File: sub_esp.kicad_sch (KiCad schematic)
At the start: 15 parts, among them J3 USB_C_Receptacle_USB2.0_14P, SW1 SW_Push, SW4 SW_Push, U6 ESP32-C3-WROOM-02, U7 BD33FC0FP

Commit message: 一部回路図変更と部品配置
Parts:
- C1: footprint Capacitor_SMD:C_0201_0603Metric_Pad0.64x0.40mm_HandSolder -> Capacitor_SMD:C_0603_1608Metric_Pad1.08x0.95mm_HandSolder
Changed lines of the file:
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@@
+					(unit 1)
+				)
+				(path "/537f457d-9719-41ea-89c7-39afb0f25936/8c87acd4-2081-458c-b251-53e233276ff2"
+					(reference "U11")
 					(unit 1)
 				)
@@
 					(unit 1)
 				)
+				(path "/537f457d-9719-41ea-89c7-39afb0f25936/8c87acd4-2081-458c-b251-53e233276ff2"
+					(reference "#PWR031")
+					(unit 1)
+				)
 			)
 		)
@@
 			)
 		)
-		(property "Footprint" "Capacitor_SMD:C_0201_0603Metric_Pad0.64x0.40mm_HandSolder"
+		(property "Footprint" "Capacitor_SMD:C_0603_1608Metric_Pad1.08x0.95mm_HandSolder"
 			(at 105.41 57.15 0)
 			(hide yes)
@@
 					(unit 1)
 				)
+				(path "/537f457d-9719-41ea-89c7-39afb0f25936/8c87acd4-2081-458c-b251-53e233276ff2"
+					(reference "C3")
+					(unit 1)
+				)
 			)
 		)
@@
 					(unit 1)
 				)
+				(path "/537f457d-9719-41ea-89c7-39afb0f25936/8c87acd4-2081-458c-b251-53e233276ff2"
+					(reference "R12")
+					(unit 1)
+				)
 			)
 		)
@@
 				(path "/537f457d-9719-41ea-89c7-39afb0f25936/1818fe2e-8d63-461c-a592-c1a19b493a42"
 					(reference "R2")
+					(unit 1)
+				)
+				(path "/537f457d-9719-41ea-89c7-39afb0f25936/8c87acd4-2081-458c-b251-53e233276ff2"
+					(reference "R10")
 					(unit 1)
 				)
@@
 					(unit 1)
 				)
+				(path "/537f457d-9719-41ea-89c7-39afb0f25936/8c87acd4-2081-458c-b251-53e233276ff2"
+					(reference "U10")
+					(unit 1)
+				)
 			)
 		)
@@
 					(unit 1)
 				)
+				(path "/537f457d-9719-41ea-89c7-39afb0f25936/8c87acd4-2081-458c-b251-53e233276ff2"
+					(reference "C4")
+					(unit 1)
+				)
 			)
 		)
@@
 					(unit 1)
 				)
+				(path "/537f457d-9719-41ea-89c7-39afb0f25936/8c87acd4-2081-458c-b251-53e233276ff2"
+					(reference "R14")
+					(unit 1)
+				)
 			)
 		)
@@
 				(path "/537f457d-9719-41ea-89c7-39afb0f25936/1818fe2e-8d63-461c-a592-c1a19b493a42"
 					(reference "R3")
+					(unit 1)
+				)
+				(path "/537f457d-9719-41ea-89c7-39afb0f25936/8c87acd4-2081-458c-b251-53e233276ff2"
+					(reference "R13")
 					(unit 1)
 				)
@@
 					(unit 1)
 				)
+				(path "/537f457d-9719-41ea-89c7-39afb0f25936/8c87acd4-2081-458c-b251-53e233276ff2"
+					(reference "#PWR041")
+					(unit 1)
+				)
 			)
 		)
@@
 					(unit 1)
 				)
+				(path "/537f457d-9719-41ea-89c7-39afb0f25936/8c87acd4-2081-458c-b251-53e233276ff2"
+					(reference "#PWR052")
+					(unit 1)
+				)
 			)
 		)
@@
 					(unit 1)
 				)
+				(path "/537f457d-9719-41ea-89c7-39afb0f25936/8c87acd4-2081-458c-b251-53e233276ff2"
+					(reference "#PWR042")
+					(unit 1)
+				)
 			)
 		)
@@
 					(unit 1)
 				)
+				(path "/537f457d-9719-41ea-89c7-39afb0f25936/8c87acd4-2081-458c-b251-53e233276ff2"
+					(reference "J4")
+					(unit 1)
+				)
 			)
 		)
@@
 					(unit 1)
 				)
+				(path "/537f457d-9719-41ea-89c7-39afb0f25936/8c87acd4-2081-458c-b251-53e233276ff2"
+					(reference "SW8")
+					(unit 1)
+				)
 			)
 		)
@@
 				(path "/537f457d-9719-41ea-89c7-39afb0f25936/1818fe2e-8d63-461c-a592-c1a19b493a42"
 					(reference "R1")
+					(unit 1)
+				)
+				(path "/537f457d-9719-41ea-89c7-39afb0f25936/8c87acd4-2081-458c-b251-53e233276ff2"
+					(reference "R9")
 					(unit 1)
 				)
@@
 					(unit 1)
 				)
+				(path "/537f457d-9719-41ea-89c7-39afb0f25936/8c87acd4-2081-458c-b251-53e233276ff2"
+					(reference "#PWR040")
+					(unit 1)
+				)
 			)
 		)
@@
 					(unit 1)
 				)
+				(path "/537f457d-9719-41ea-89c7-39afb0f25936/8c87acd4-2081-458c-b251-53e233276ff2"
+					(reference "#PWR039")
+					(unit 1)
+				)
 			)
 		)
@@
 					(unit 1)
 				)
+				(path "/537f457d-9719-41ea-89c7-39afb0f25936/8c87acd4-2081-458c-b251-53e233276ff2"
+					(reference "#PWR034")
+					(unit 1)
+				)
 			)
 		)
@@
 					(unit 1)
 				)
+				(path "/537f457d-9719-41ea-89c7-39afb0f25936/8c87acd4-2081-458c-b251-53e233276ff2"
+					(reference "D7")
+					(unit 1)
+				)
 			)
 		)
@@
 					(unit 1)
 				)
+				(path "/537f457d-9719-41ea-89c7-39afb0f25936/8c87acd4-2081-458c-b251-53e233276ff2"
+					(reference "#PWR044")
+					(unit 1)
+				)
 			)
 		)
@@
 					(unit 1)
 				)
+				(path "/537f457d-9719-41ea-89c7-39afb0f25936/8c87acd4-2081-458c-b251-53e233276ff2"
+					(reference "SW7")
+					(unit 1)
+				)
 			)
 		)
@@
 					(unit 1)
 				)
+				(path "/537f457d-9719-41ea-89c7-39afb0f25936/8c87acd4-2081-458c-b251-53e233276ff2"
+					(reference "#PWR051")
+					(unit 1)
+				)
 			)
 		)
@@
 				(path "/537f457d-9719-41ea-89c7-39afb0f25936/1818fe2e-8d63-461c-a592-c1a19b493a42"
 					(reference "C25")
+					(unit 1)
+				)
+				(path "/537f457d-9719-41ea-89c7-39afb0f25936/8c87acd4-2081-458c-b251-53e233276ff2"
+					(reference "C27")
 					(unit 1)
 				)
@@
 					(unit 1)
 				)
+				(path "/537f457d-9719-41ea-89c7-39afb0f25936/8c87acd4-2081-458c-b251-53e233276ff2"
+					(reference "C28")
+					(unit 1)
+				)
 			)
 		)
@@
 					(unit 1)
 				)
+				(path "/537f457d-9719-41ea-89c7-39afb0f25936/8c87acd4-2081-458c-b251-53e233276ff2"
+					(reference "#PWR050")
+					(unit 1)
+				)
 			)
 		)
@@
 					(unit 1)
 				)
+				(path "/537f457d-9719-41ea-89c7-39afb0f25936/8c87acd4-2081-458c-b251-53e233276ff2"
+					(reference "#PWR032")
+					(unit 1)
+				)

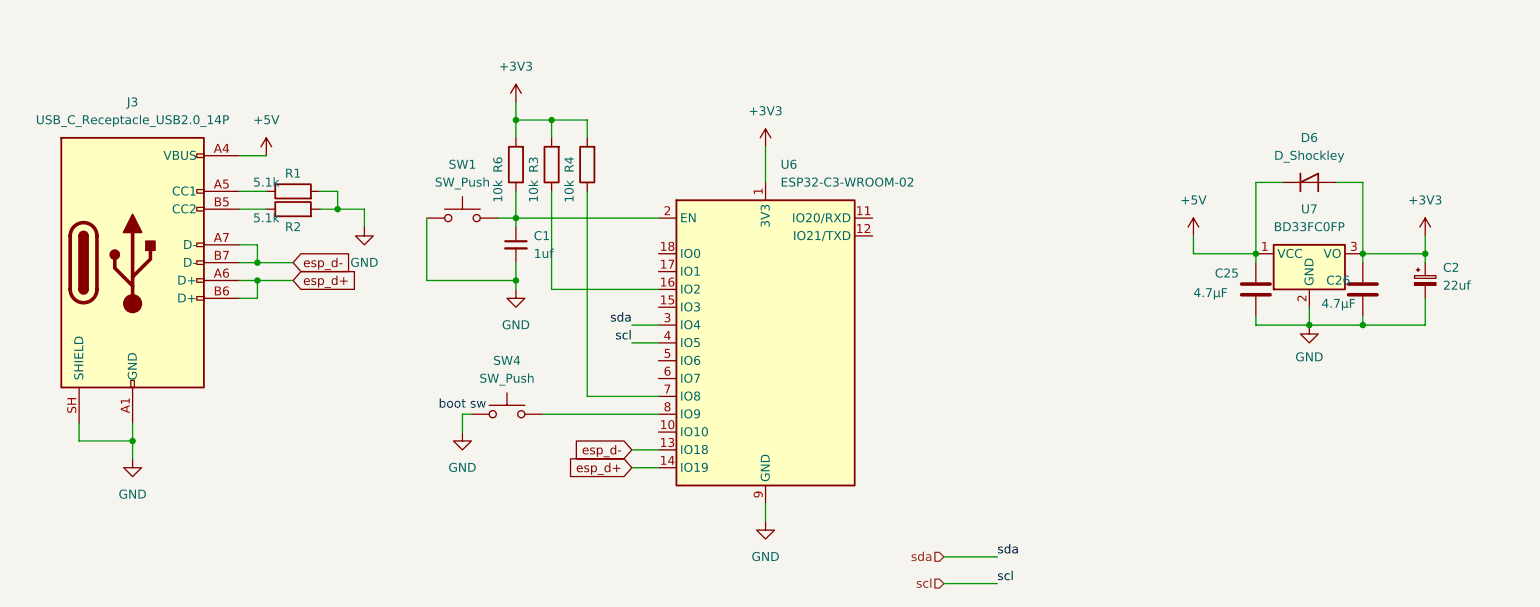
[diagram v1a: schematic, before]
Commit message: 完成(電磁弁制御,モーター出力追加済み)
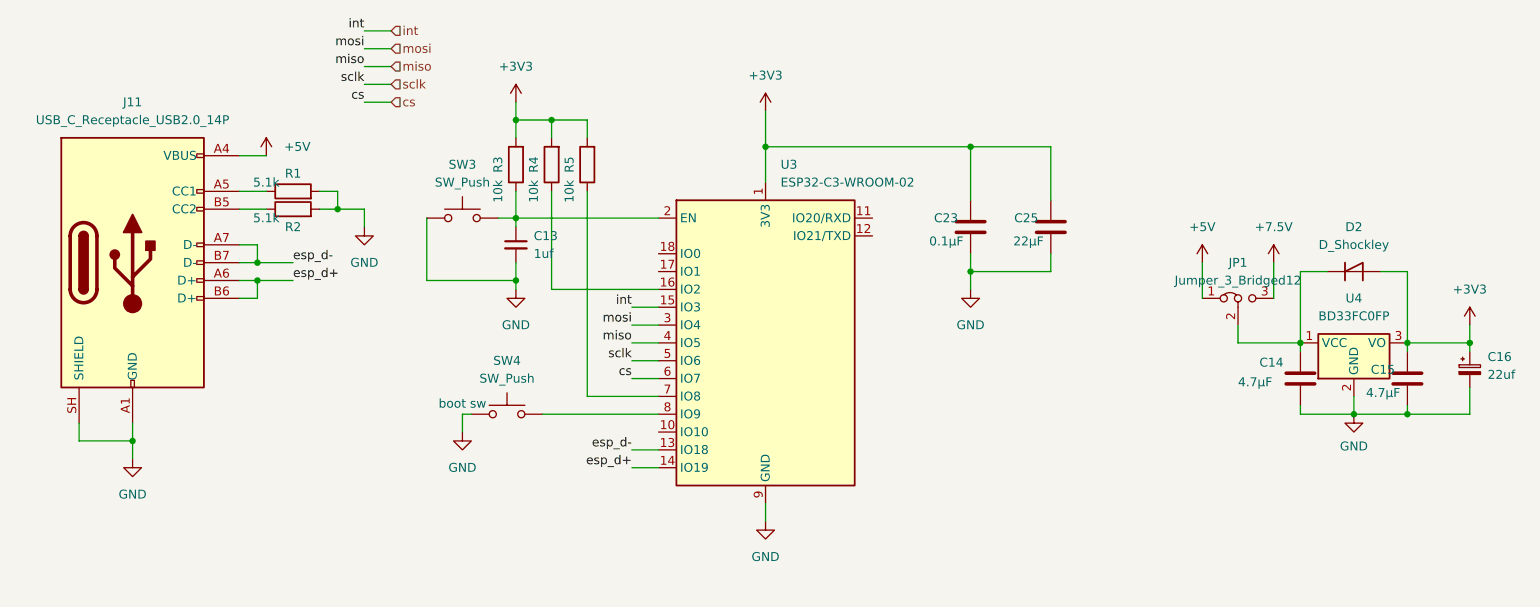
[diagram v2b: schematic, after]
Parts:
- added C23: 0.1μF, Capacitor_SMD:C_0603_1608Metric, symbol Device:C
- added C25: 22μF, Capacitor_SMD:C_0805_2012Metric_Pad1.18x1.45mm_HandSolder, symbol Device:C
- added JP1: Jumper_3_Bridged12, Connector_PinHeader_2.54mm:PinHeader_1x03_P2.54mm_Vertical, symbol Jumper:Jumper_3_Bridged12
- R3: renamed from R6; footprint Resistor_SMD:R_0603_1608Metric_Pad0.98x0.95mm_HandSolder -> Resistor_SMD:R_0805_2012Metric
- R4: renamed from R3; footprint Resistor_SMD:R_0603_1608Metric_Pad0.98x0.95mm_HandSolder -> Resistor_SMD:R_0805_2012Metric
- R5: renamed from R4; footprint Resistor_SMD:R_0603_1608Metric_Pad0.98x0.95mm_HandSolder -> Resistor_SMD:R_0805_2012Metric
- SW3: renamed from SW1; footprint Button_Switch_THT:SW_PUSH_6mm -> Button_Switch_SMD:SW_Push_SPST_NO_Alps_SKRK
- SW4: footprint Button_Switch_THT:SW_PUSH_6mm -> Button_Switch_SMD:SW_Push_SPST_NO_Alps_SKRK
- renumbered C1 to C13, C25 to C14, C26 to C15, C2 to C16, D6 to D2, J3 to J11, U6 to U3, U7 to U4
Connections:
- net +3V3: now also C23.1, C25.1
- net +5V: now also JP1.1 (A); no longer C14.1, D2.1 (K), U4.1 (VCC)
- net GND: now also C23.2, C25.2
- net int: now reaches U3.15 (IO3)
- net sclk: now reaches U3.5 (IO6)
- net cs: now reaches U3.6 (IO7)
- net scl renamed miso
- net sda renamed mosi
- new net: C14.1, D2.1 (K), JP1.2 (C), U4.1 (VCC)
- new net +7.5V: JP1.3 (B)
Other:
- moved on the sheet: C14, C15, C16, D2, U4

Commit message: サーボときんていをつけ忘れていたので回路図に追加(部品配置に悩んでる
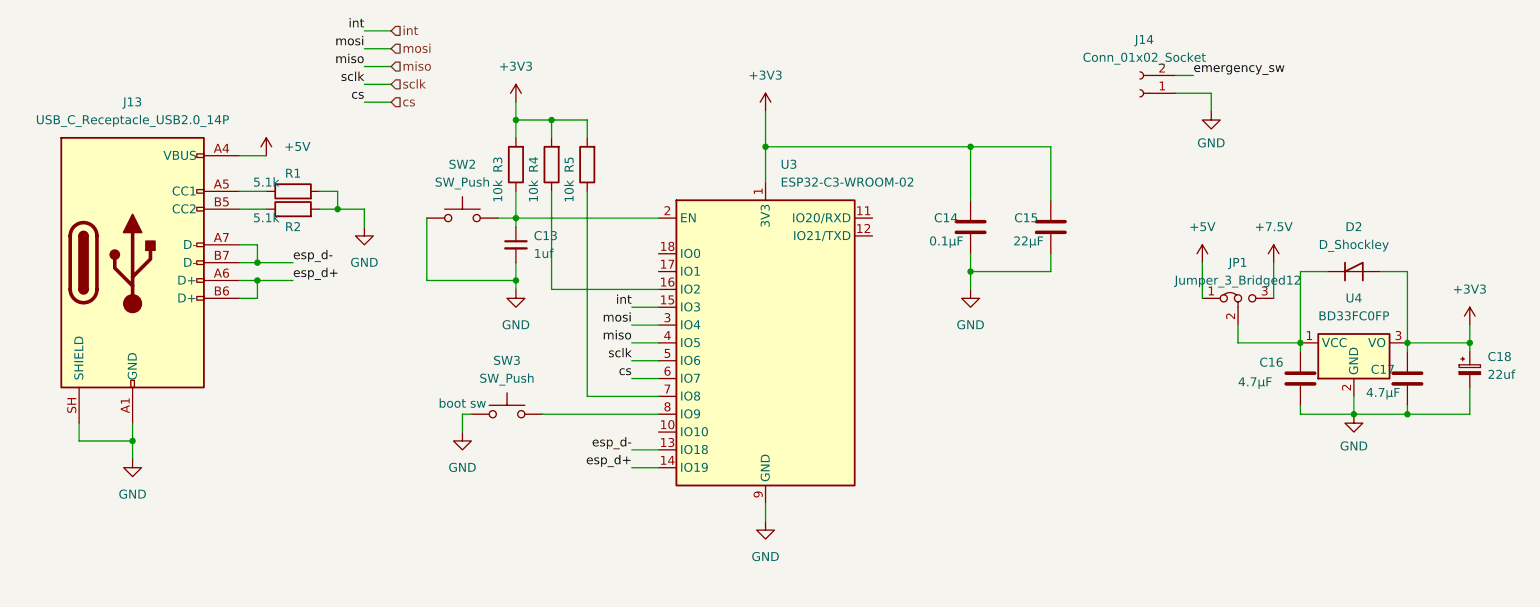
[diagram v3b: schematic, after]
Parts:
- added J14: Conn_01x02_Socket, Connector_JST:JST_XH_S2B-XH-A-1_1x02_P2.50mm_Horizontal, symbol Connector:Conn_01x02_Socket
- renumbered C23 to C14, C25 to C15, C14 to C16, C15 to C17, C16 to C18, J11 to J13, SW3 to SW2, SW4 to SW3
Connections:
- net GND: now also J14.1 (Pin_1)
- new net emergency_sw: J14.2 (Pin_2)

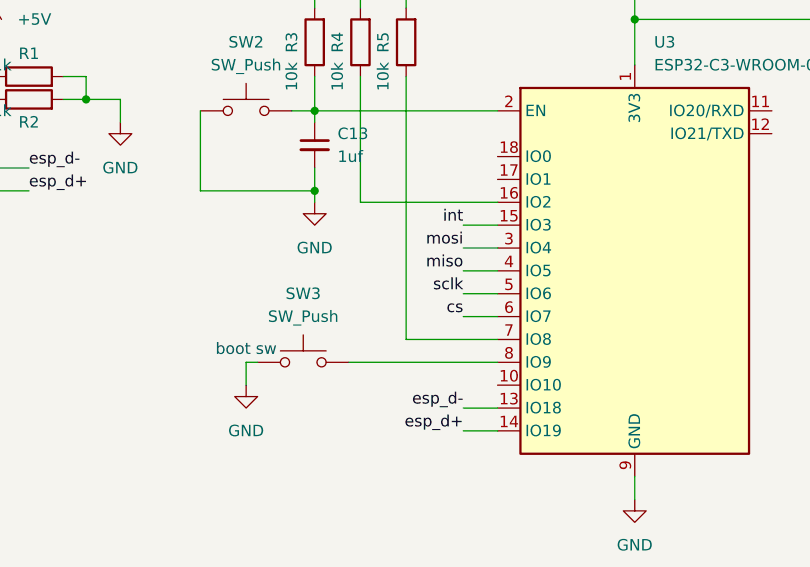
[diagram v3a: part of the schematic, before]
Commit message: サーボ系ときんてい系の部品の配置と配線
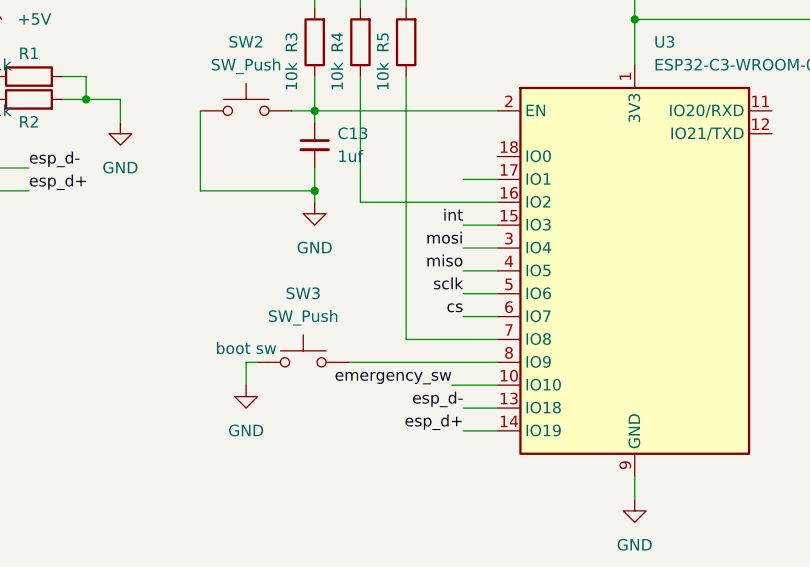
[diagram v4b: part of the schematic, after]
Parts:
- J14: footprint Connector_JST:JST_XH_S2B-XH-A-1_1x02_P2.50mm_Horizontal -> Connector_JST:JST_XH_B2B-XH-A_1x02_P2.50mm_Vertical
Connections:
- net emergency_sw: now also U3.10 (IO10)
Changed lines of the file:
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@@
+	(wire
+		(pts
+			(xy 121.92 60.96) (xy 125.73 60.96)
+		)
+		(stroke
+			(width 0)
+			(type default)
+		)
+	)
 	(wire
 		(pts
@@
 		(pts
 			(xy 105.41 54.61) (xy 105.41 53.34)
+		)
+		(stroke
+			(width 0)
+			(type default)
+		)
+	)
+	(wire
+		(pts
+			(xy 120.65 83.82) (xy 125.73 83.82)
 		)
 		(stroke
@@
 	(label "sclk"
 		(at 83.82 34.29 180)
+		(effects
+			(font
+				(size 1.27 1.27)
+			)
+			(justify right bottom)
+		)
+	)
+	(label "emergency_sw"
+		(at 120.65 83.82 180)
 		(effects
 			(font
@@
 			)
 		)
-		(property "Footprint" "Connector_JST:JST_XH_S2B-XH-A-1_1x02_P2.50mm_Horizontal"
+		(property "Footprint" "Connector_JST:JST_XH_B2B-XH-A_1x02_P2.50mm_Vertical"
 			(at 194.31 35.56 0)
 			(hide yes)
